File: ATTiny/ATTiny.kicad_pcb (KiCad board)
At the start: 2 copper layers, 23 x 27 mm, 6 parts, among them J1 Screw_Terminal_2x2.54, J6 Conn_01x06_Female, U2 ATtiny85-20P

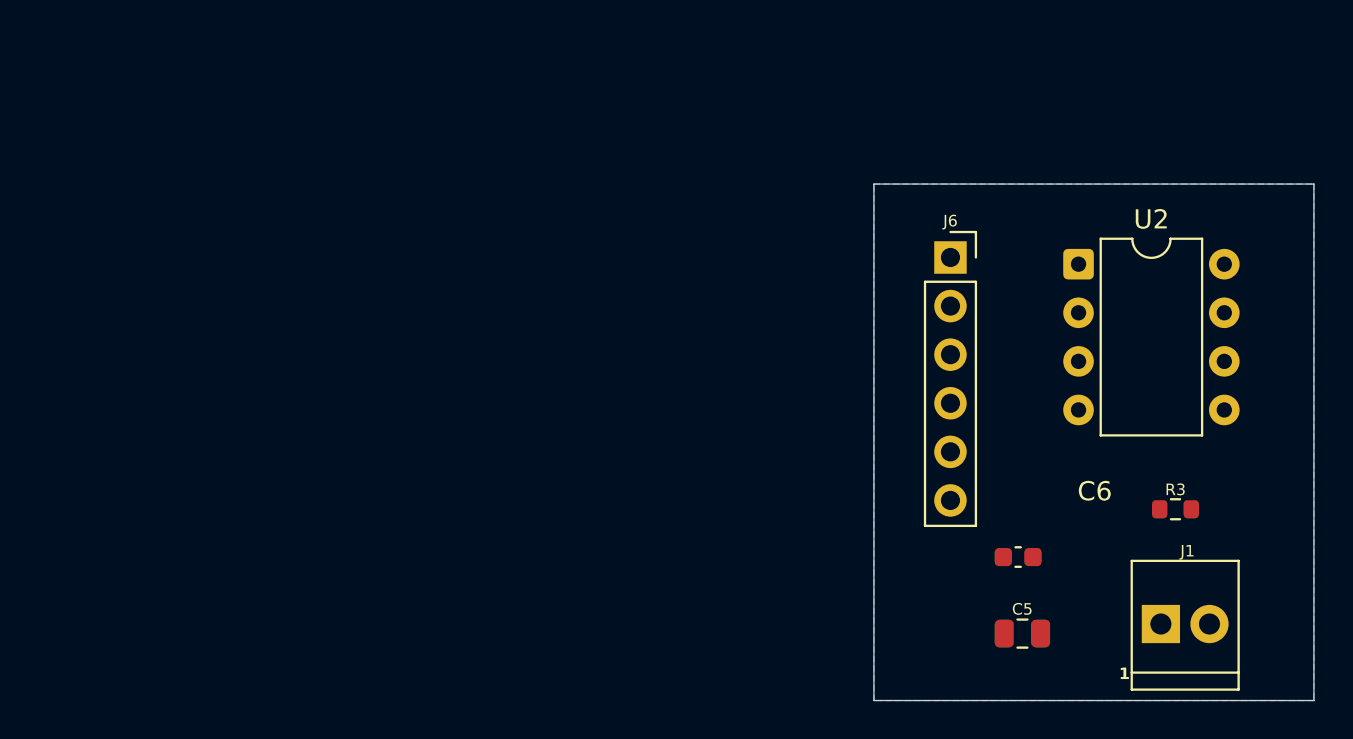
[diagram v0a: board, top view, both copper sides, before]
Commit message: Changed for ATTiny Socket & Arduino Header Stacking
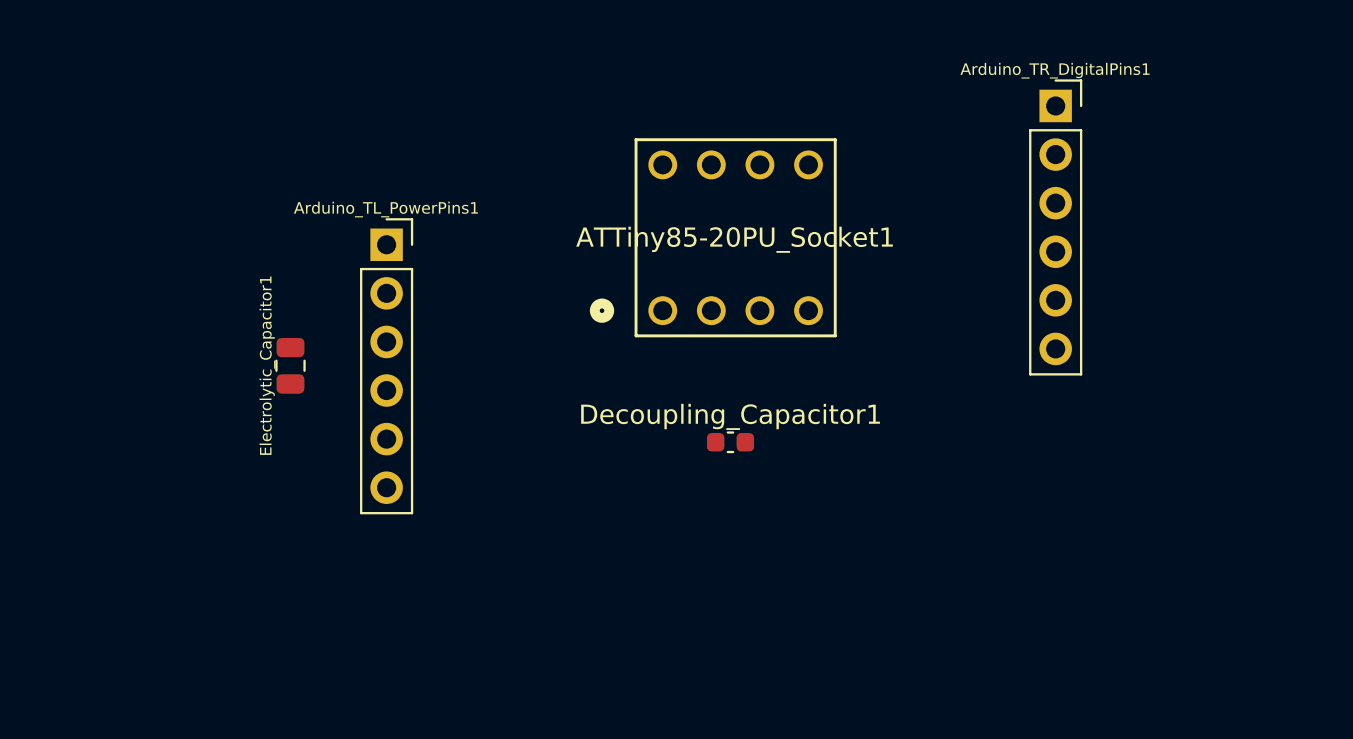
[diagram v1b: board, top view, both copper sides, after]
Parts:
- removed C5: 10u, rsx_capacitors:C_0805_2012Metric
- removed C6: 100n, Capacitor_SMD:C_0603_1608Metric
- removed J1: Screw_Terminal_2x2.54, rsx_headers_screw:Wurth_691210910002
- removed J6: Conn_01x06_Female, rsx_headers:PinSocket_1x06_P2.54mm_Vertical
- removed R3: 10k, rsx_resistors:R_0603_1608Metric
- removed U2: ATtiny85-20P, Package_DIP:DIP-8_W7.62mm
- added ATTiny85-20PU_Socket1: ic_conn_8pin, rsx_misc:CONN8_1-2199298-2_TEC, F.Cu at (45.0, 30.6)
- added Arduino_TL_PowerPins1: Conn_01x06_Female, rsx_headers:PinSocket_1x06_P2.54mm_Vertical, F.Cu at (30.5, 27.2)
- added Arduino_TR_DigitalPins1: Conn_01x06_Female, rsx_headers:PinSocket_1x06_P2.54mm_Vertical, F.Cu at (65.5, 19.9)
- added Decoupling_Capacitor1: 100n, Capacitor_SMD:C_0603_1608Metric, F.Cu at (48.5, 37.5)
- added Electrolytic_Capacitor1: 10u, rsx_capacitors:C_0805_2012Metric, F.Cu at (25.5, 33.5)
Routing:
- removed copper zone on B.Cu, net GND
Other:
- board outline removed

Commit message: Adj ATTiny
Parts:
- removed Electrolytic_Capacitor1: 10u, rsx_capacitors:C_0805_2012Metric
- added Electrolytic_Capacitor_Arduino1: 10u, rsx_capacitors:C_0805_2012Metric, F.Cu at (42.4, 36.2)
- added R1: 10k, rsx_resistors:R_0603_1608Metric, F.Cu at (38.2, 38.4)
- moved Arduino_TR_DigitalPins1 31.9 mm to (33.9, 24.3)
- moved Decoupling_Capacitor1 10.4 mm to (38.2, 35.9)
- moved ATTiny85-20PU_Socket1 4.57 mm to (40.5, 31.6)
- moved Arduino_TL_PowerPins1 3.09 mm to (29.3, 24.3)
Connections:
- net /10_Pin1_RESET renamed /RESET
- net /11_Pin5_MOSI renamed /MOSI
- net /12_Pin6_MISO renamed /MISO
- net /5V_Pin8 renamed /5V
- net /GND_Pin4 renamed /GND
- ATTiny85-20PU_Socket1 pad 7: /13_Pin7_SCK -> /SCK
- Arduino_TR_DigitalPins1 pad 1: /13_Pin7_SCK -> Net-(Arduino_TR_DigitalPins1-Pin_1)

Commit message: header pins complete
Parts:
- moved Electrolytic_Capacitor_Arduino1 9.20 mm to (50.0, 41.5)
- moved R1 8.43 mm to (42.8, 45.5)
- moved Decoupling_Capacitor1 7.20 mm to (42.8, 41.5)
- moved Arduino_TR_DigitalPins1 6.44 mm to (37.5, 29.7)
- moved ATTiny85-20PU_Socket1 6.37 mm to (44.0, 37.0)
- moved Arduino_TL_PowerPins1 6.37 mm to (32.8, 29.7)
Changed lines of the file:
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@@
 	(footprint "rsx_headers:PinSocket_1x06_P2.54mm_Vertical"
 		(layer "F.Cu")
-		(at 29.325 24.325)
+		(at 32.775 29.6848)
 		(descr "Through hole straight socket strip, 1x06, 2.54mm pitch, single row (from Kicad 4.0.7), script generated")
 		(tags "Through hole socket strip THT 1x06 2.54mm single row")
@@
 	(footprint "rsx_resistors:R_0603_1608Metric"
 		(layer "F.Cu")
-		(at 38.205 38.445)
+		(at 42.825 45.5)
 		(descr "Resistor SMD 0603 (1608 Metric), square (rectangular) end terminal, IPC_7351 nominal, (Body size source: IPC-SM-782 page 72, https://www.pcb-3d.com/wordpress/wp-content/uploads/ipc-sm-782a_amendment_1_and_2.pdf), generated with kicad-footprint-generator")
 		(tags "resistor")
@@
 	(footprint "rsx_capacitors:C_0805_2012Metric"
 		(layer "F.Cu")
-		(at 42.435 36.185)
+		(at 49.95 41.5)
 		(descr "Capacitor SMD 0805 (2012 Metric), square (rectangular) end terminal, IPC_7351 nominal, (Body size source: IPC-SM-782 page 76, https://www.pcb-3d.com/wordpress/wp-content/uploads/ipc-sm-782a_amendment_1_and_2.pdf, https://docs.google.com/spreadsheets/d/1BsfQQcO9C6DZCsRaXUlFlo91Tg2WpOkGARC1WS5S8t0/edit?usp=sharing), generated with kicad-footprint-generator")
 		(tags "capacitor")
@@
 	(footprint "rsx_misc:CONN8_1-2199298-2_TEC"
 		(layer "F.Cu")
-		(at 40.51 31.6402)
+		(at 43.96 37)
 		(tags "1-2199298-2 ")
 		(property "Reference" "ATTiny85-20PU_Socket1"
@@
 	(footprint "rsx_headers:PinSocket_1x06_P2.54mm_Vertical"
 		(layer "F.Cu")
-		(at 33.925 24.325)
+		(at 37.5 29.6848)
 		(descr "Through hole straight socket strip, 1x06, 2.54mm pitch, single row (from Kicad 4.0.7), script generated")
 		(tags "Through hole socket strip THT 1x06 2.54mm single row")
@@
 	(footprint "Capacitor_SMD:C_0603_1608Metric"
 		(layer "F.Cu")
-		(at 38.205 35.935)
+		(at 42.775 41.5)
 		(descr "Capacitor SMD 0603 (1608 Metric), square (rectangular) end terminal, IPC-7351 nominal, (Body size source: IPC-SM-782 page 76, https://www.pcb-3d.com/wordpress/wp-content/uploads/ipc-sm-782a_amendment_1_and_2.pdf)")
 		(tags "capacitor")

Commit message: ATTiny Adjust
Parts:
- removed Arduino_TL_PowerPins1, Arduino_TR_DigitalPins1: Conn_01x06_Female, rsx_headers:PinSocket_1x06_P2.54mm_Vertical
- removed R1: 10k, rsx_resistors:R_0603_1608Metric
- added Arduino_BL1: header_1x6_arduino, Connector_PinHeader_2.54mm:PinHeader_1x06_P2.54mm_Vertical, F.Cu at (30.5, 19.8)
- added Arduino_BR1: header_1x8_arduino, Connector_PinHeader_2.54mm:PinHeader_1x08_P2.54mm_Vertical, F.Cu at (21.3, 19.8)
- added Arduino_TL1: header_1x8_arduino, Connector_PinHeader_2.54mm:PinHeader_1x08_P2.54mm_Vertical, F.Cu at (25.9, 19.8)
- added Arduino_TR_1: header_1x4_arduino, Connector_PinHeader_2.54mm:PinHeader_1x04_P2.54mm_Vertical, F.Cu at (39.7, 19.8)
- added Arduino_TR_2: header_1x6_arduino, Connector_PinHeader_2.54mm:PinHeader_1x06_P2.54mm_Vertical, F.Cu at (35.1, 19.8)
- added R2: 10k, rsx_resistors:R_0603_1608Metric, F.Cu at (39.4, 33.5)
- moved Electrolytic_Capacitor_Arduino1 28.7 mm to (21.2, 41.4)
- moved ATTiny85-20PU_Socket1 13.7 mm to (32.5, 44.4)
- moved Decoupling_Capacitor1 11.1 mm to (39.4, 31.0)
